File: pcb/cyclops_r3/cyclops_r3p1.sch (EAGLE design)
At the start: 70 parts, among them Q1 SUM11006, Q2 IRF510, U1 MCP4921, U2 317-N, U3 ADR03, U4 OP1177, U5 LM324N, U6 ZXTD45, U8 TLV3701CDBVT

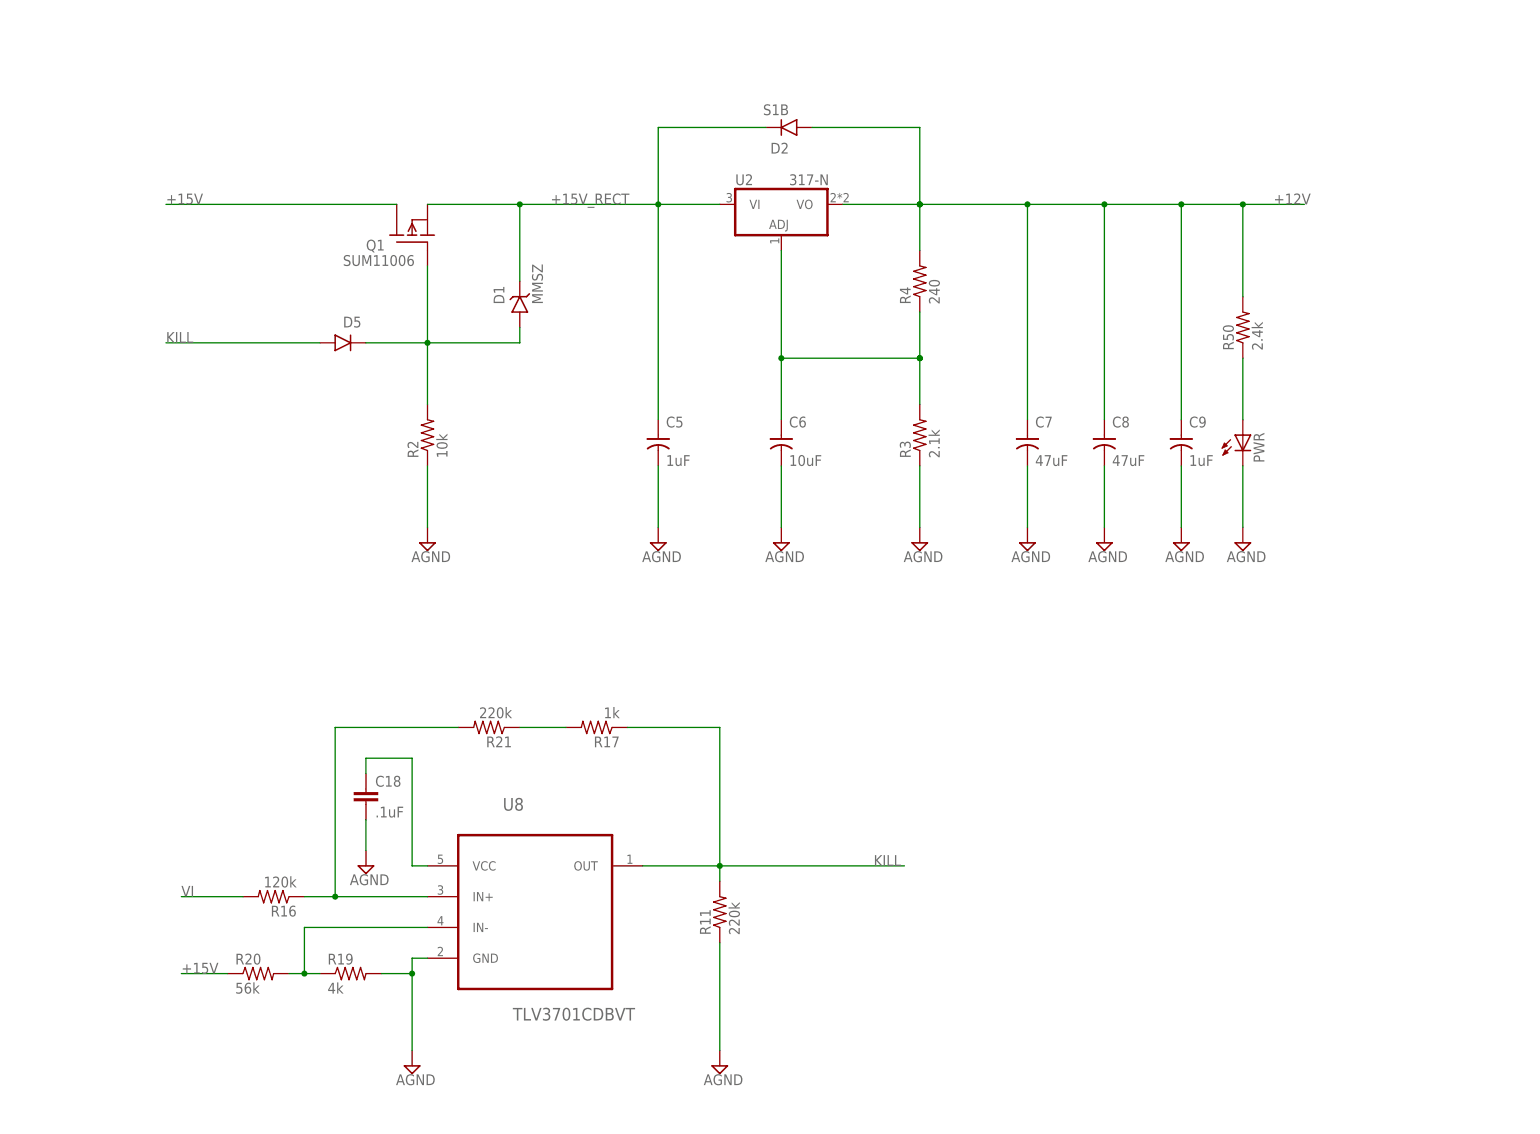
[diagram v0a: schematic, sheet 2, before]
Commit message: Modifications to overcurrent protection allow 2A max, and lights alarm LED.
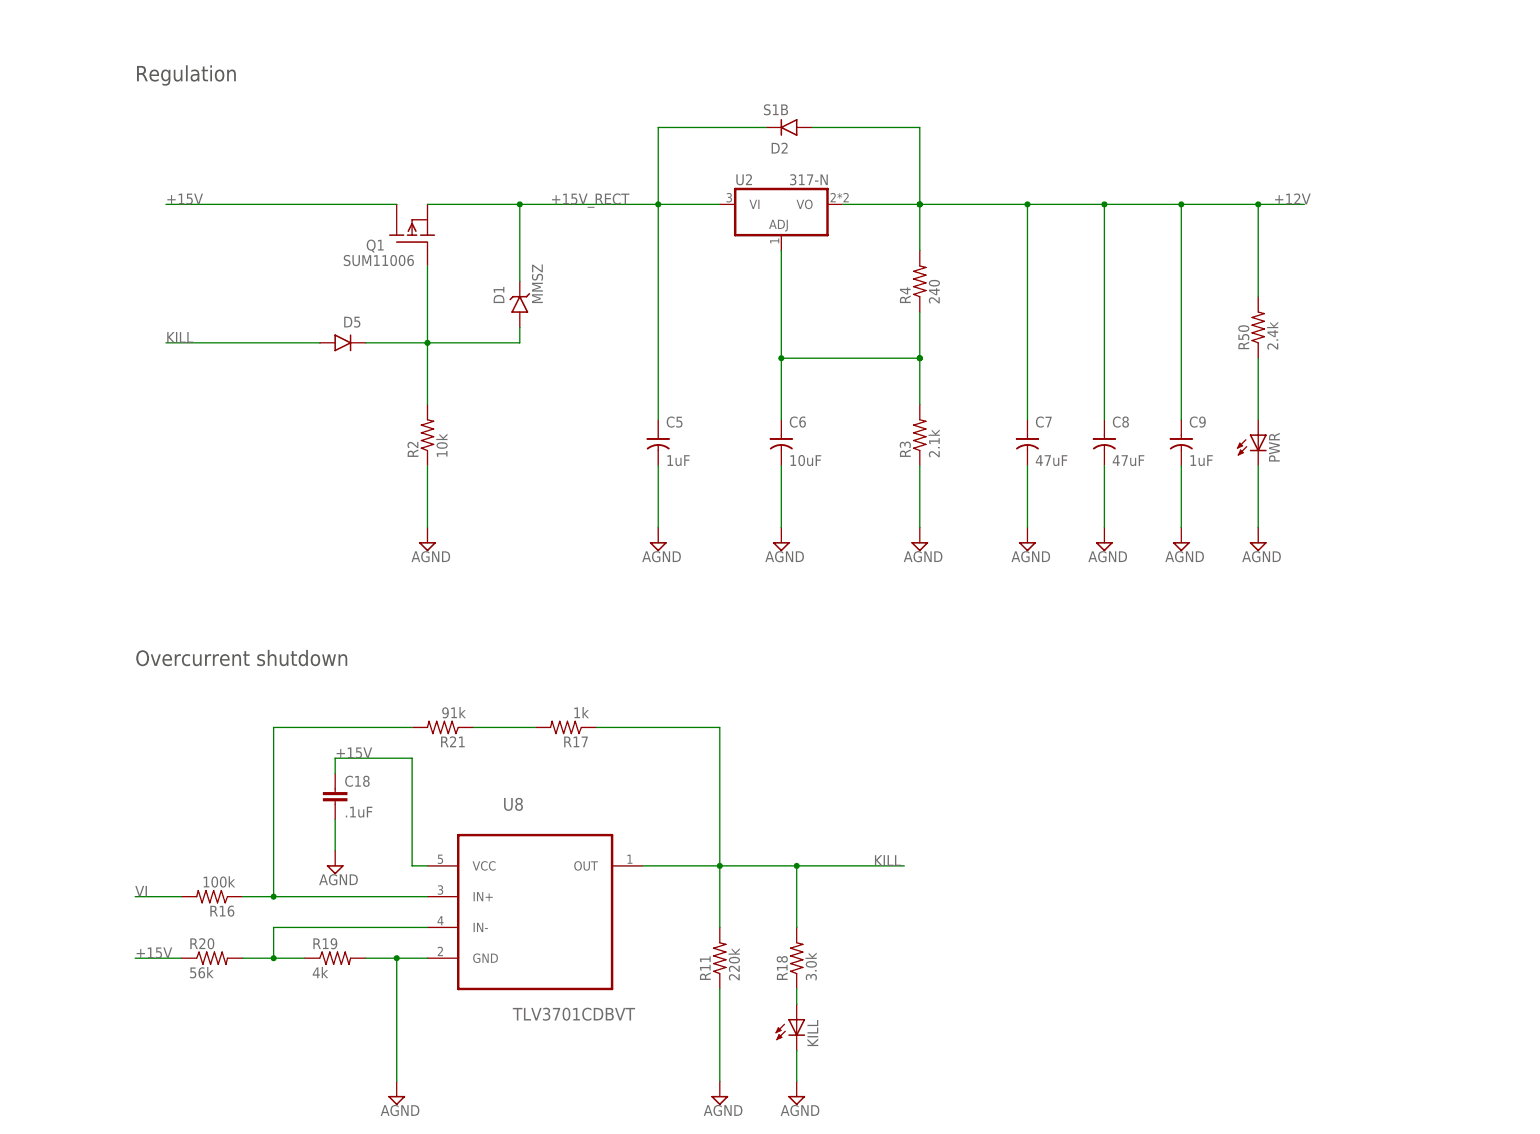
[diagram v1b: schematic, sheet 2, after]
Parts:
- added KILL: (no value), cyclops:LEDYELLOW_0805
- added R18: 3.0k, cyclops:R_0603
- R16: value 120k -> 100k
- R21: value 220k -> 91k
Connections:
- new net N$11: KILL.A, R18.1
- net GND: now also KILL.C
- net KILL: now also R18.2
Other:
- note added: "Board Temperature"
- note added: "I/O and DAC"
- note added: "Overcurrent shutdown"
- note added: "Reference voltage"
- note added: "Regulation"
- moved on the sheet: C18, PWR, R11, R16, R17, R19, R20, R21, R50

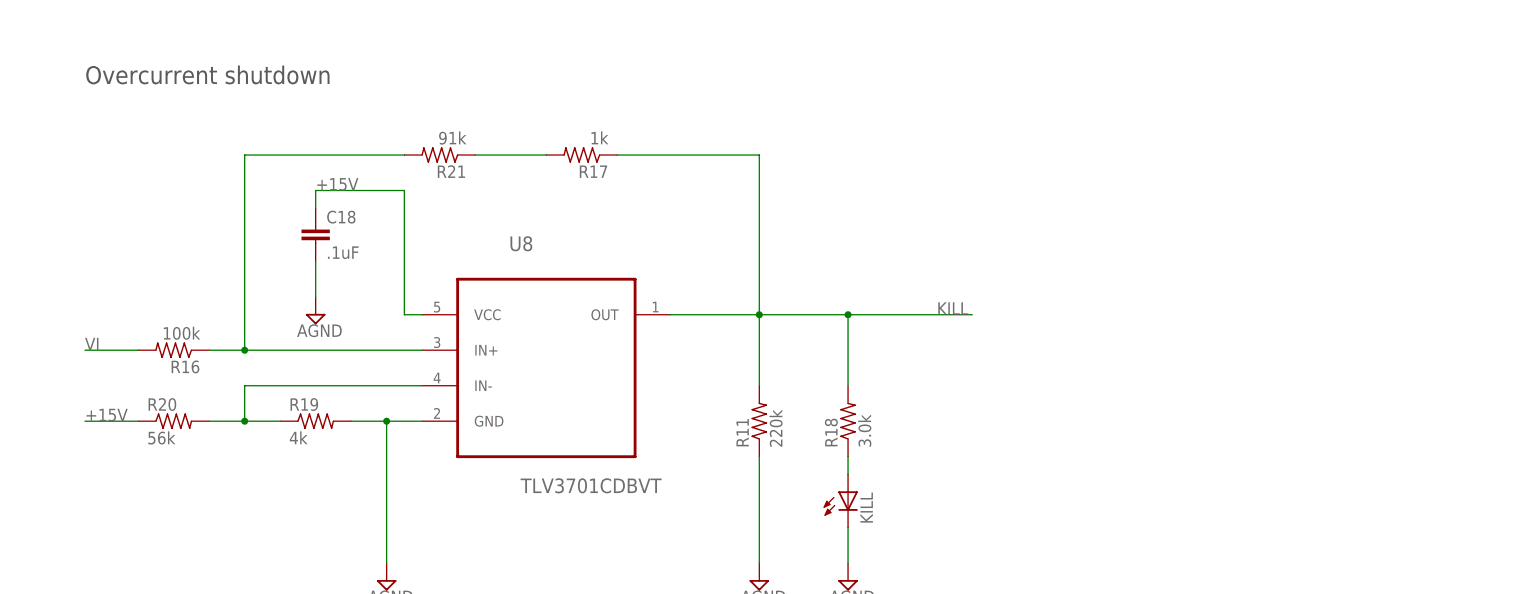
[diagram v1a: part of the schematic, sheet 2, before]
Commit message: Started implementing the over curren protection circuit on the board.
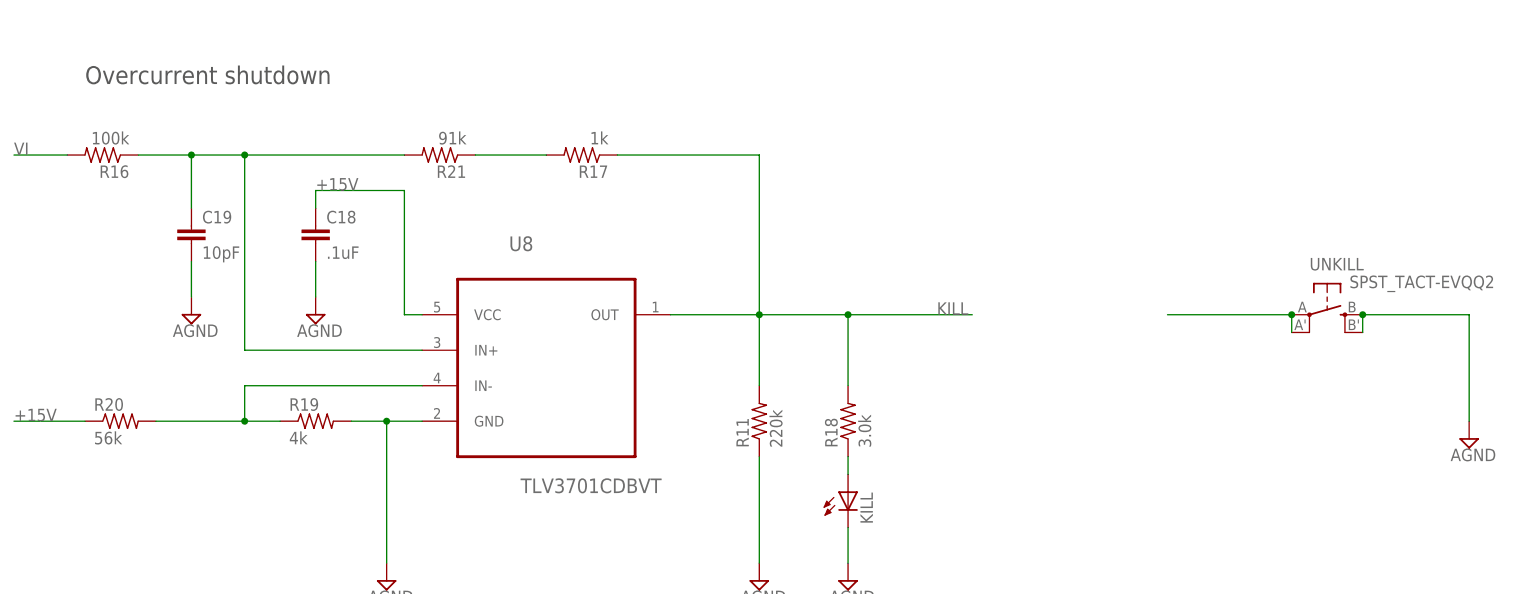
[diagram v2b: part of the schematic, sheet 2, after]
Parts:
- added C19: 10pF, cyclops:C_0603
- added UNKILL: SPST_TACT-EVQQ2, cyclops:SPST_TACT-EVQQ2
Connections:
- removed net N$14: R16.1, R21.2, U8.IN+
- new net COMP+: C19.1, R16.1, R21.2, U8.IN+, UNKILL.P, UNKILL.P1
- net AGND: now also UNKILL.S, UNKILL.S1
- net GND: now also C19.2
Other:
- moved on the sheet: R16, R20
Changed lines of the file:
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@@
 <part name="KILL" library="cyclops" deviceset="LED" device="_0805" technology="YELLOW"/>
 <part name="SUPPLY44" library="supply2" deviceset="AGND" device=""/>
+<part name="C19" library="cyclops" deviceset="C" device="_0603" value="10pF"/>
+<part name="SUPPLY45" library="cyclops" deviceset="AGND" device=""/>
+<part name="UNKILL" library="cyclops" deviceset="SPST_TACT" device="-EVQQ2"/>
+<part name="SUPPLY46" library="supply2" deviceset="AGND" device=""/>
 </parts>
 <sheets>
@@
 <attribute name="VALUE" x="-44.45" y="-99.822" size="1.778" layer="96"/>
 </instance>
-<instance part="R20" gate="R" x="-60.96" y="-96.52" smashed="yes">
-<attribute name="NAME" x="-64.77" y="-95.0214" size="1.778" layer="95"/>
-<attribute name="VALUE" x="-64.77" y="-99.822" size="1.778" layer="96"/>
+<instance part="R20" gate="R" x="-68.58" y="-96.52" smashed="yes">
+<attribute name="NAME" x="-72.39" y="-95.0214" size="1.778" layer="95"/>
+<attribute name="VALUE" x="-72.39" y="-99.822" size="1.778" layer="96"/>
 </instance>
 <instance part="R21" gate="R" x="-22.86" y="-58.42" smashed="yes" rot="R180">
@@
 <attribute name="VALUE" x="-19.05" y="-55.118" size="1.778" layer="96" rot="R180"/>
 </instance>
-<instance part="R16" gate="R" x="-60.96" y="-86.36" smashed="yes" rot="R180">
-<attribute name="NAME" x="-57.15" y="-87.8586" size="1.778" layer="95" rot="R180"/>
-<attribute name="VALUE" x="-57.15" y="-83.058" size="1.778" layer="96" rot="R180"/>
+<instance part="R16" gate="R" x="-71.12" y="-58.42" smashed="yes" rot="R180">
+<attribute name="NAME" x="-67.31" y="-59.9186" size="1.778" layer="95" rot="R180"/>
+<attribute name="VALUE" x="-67.31" y="-55.118" size="1.778" layer="96" rot="R180"/>
 </instance>
 <instance part="SUPPLY41" gate="G$1" x="22.86" y="-119.38"/>
@@
 <instance part="KILL" gate="G$1" x="35.56" y="-106.68"/>
 <instance part="SUPPLY44" gate="G$1" x="35.56" y="-119.38"/>
+<instance part="C19" gate="C" x="-58.42" y="-68.58"/>
+<instance part="SUPPLY45" gate="G$1" x="-58.42" y="-81.28"/>
+<instance part="UNKILL" gate="G$1" x="104.14" y="-81.28" rot="R270"/>
+<instance part="SUPPLY46" gate="G$1" x="124.46" y="-99.06"/>
 </instances>
 <busses>
@@
 <segment>
 <pinref part="R20" gate="R" pin="1"/>
-<wire x1="-66.04" y1="-96.52" x2="-73.66" y2="-96.52" width="0.1524" layer="91"/>
-<label x="-73.66" y="-96.52" size="1.778" layer="95"/>
+<wire x1="-73.66" y1="-96.52" x2="-83.82" y2="-96.52" width="0.1524" layer="91"/>
+<label x="-83.82" y="-96.52" size="1.778" layer="95"/>
 </segment>
 <segment>
@@
 <wire x1="35.56" y1="-111.76" x2="35.56" y2="-116.84" width="0.1524" layer="91"/>
 </segment>
+<segment>
+<pinref part="SUPPLY45" gate="G$1" pin="AGND"/>
+<pinref part="C19" gate="C" pin="2"/>
+<wire x1="-58.42" y1="-78.74" x2="-58.42" y2="-73.66" width="0.1524" layer="91"/>
+</segment>
 </net>
 <net name="N$18" class="0">
@@
 </segment>
 </net>
-<net name="N$14" class="0">
-<segment>
-<pinref part="U8" gate="A" pin="IN+"/>
-<wire x1="-25.4" y1="-86.36" x2="-50.8" y2="-86.36" width="0.1524" layer="91"/>
-<wire x1="-50.8" y1="-86.36" x2="-50.8" y2="-58.42" width="0.1524" layer="91"/>
-<wire x1="-50.8" y1="-58.42" x2="-27.94" y2="-58.42" width="0.1524" layer="91"/>
-<pinref part="R16" gate="R" pin="1"/>
-<wire x1="-55.88" y1="-86.36" x2="-50.8" y2="-86.36" width="0.1524" layer="91"/>
-<junction x="-50.8" y="-86.36"/>
-<pinref part="R21" gate="R" pin="2"/>
-</segment>
-</net>
 <net name="N$5" class="0">
 <segment>
 <pinref part="R20" gate="R" pin="2"/>
 <pinref part="R19" gate="R" pin="1"/>
-<wire x1="-55.88" y1="-96.52" x2="-50.8" y2="-96.52" width="0.1524" layer="91"/>
+<wire x1="-63.5" y1="-96.52" x2="-50.8" y2="-96.52" width="0.1524" layer="91"/>
 <wire x1="-50.8" y1="-96.52" x2="-45.72" y2="-96.52" width="0.1524" layer="91"/>
 <wire x1="-50.8" y1="-96.52" x2="-50.8" y2="-91.44" width="0.1524" layer="91"/>
@@
 <segment>
 <pinref part="R16" gate="R" pin="2"/>
-<wire x1="-66.04" y1="-86.36" x2="-73.66" y2="-86.36" width="0.1524" layer="91"/>
-<label x="-73.66" y="-86.36" size="1.778" layer="95"/>
+<wire x1="-76.2" y1="-58.42" x2="-83.82" y2="-58.42" width="0.1524" layer="91"/>
+<label x="-83.82" y="-58.42" size="1.778" layer="95"/>
 </segment>
 </net>
@@
 </segment>
 </net>
+<net name="COMP+" class="0">
+<segment>
+<pinref part="UNKILL" gate="G$1" pin="P"/>
+<wire x1="81.28" y1="-81.28" x2="99.06" y2="-81.28" width="0.1524" layer="91"/>
+<pinref part="UNKILL" gate="G$1" pin="P1"/>
+<wire x1="99.06" y1="-81.28" x2="99.06" y2="-83.82" width="0.1524" layer="91"/>
+<junction x="99.06" y="-81.28"/>
+</segment>
+<segment>
+<pinref part="U8" gate="A" pin="IN+"/>
+<wire x1="-25.4" y1="-86.36" x2="-50.8" y2="-86.36" width="0.1524" layer="91"/>
+<wire x1="-50.8" y1="-86.36" x2="-50.8" y2="-58.42" width="0.1524" layer="91"/>
+<wire x1="-50.8" y1="-58.42" x2="-27.94" y2="-58.42" width="0.1524" layer="91"/>
+<pinref part="R16" gate="R" pin="1"/>
+<wire x1="-66.04" y1="-58.42" x2="-58.42" y2="-58.42" width="0.1524" layer="91"/>
+<junction x="-50.8" y="-58.42"/>
+<pinref part="R21" gate="R" pin="2"/>
+<pinref part="C19" gate="C" pin="1"/>
+<wire x1="-58.42" y1="-58.42" x2="-50.8" y2="-58.42" width="0.1524" layer="91"/>
+<wire x1="-58.42" y1="-66.04" x2="-58.42" y2="-58.42" width="0.1524" layer="91"/>
+<junction x="-58.42" y="-58.42"/>
+</segment>
+</net>
+<net name="AGND" class="0">
+<segment>
+<pinref part="UNKILL" gate="G$1" pin="S1"/>
+<pinref part="UNKILL" gate="G$1" pin="S"/>
+<wire x1="109.22" y1="-83.82" x2="109.22" y2="-81.28" width="0.1524" layer="91"/>
+<wire x1="109.22" y1="-81.28" x2="124.46" y2="-81.28" width="0.1524" layer="91"/>
+<junction x="109.22" y="-81.28"/>
+<wire x1="124.46" y1="-81.28" x2="124.46" y2="-96.52" width="0.1524" layer="91"/>
+<pinref part="SUPPLY46" gate="G$1" pin="AGND"/>
+</segment>
+</net>

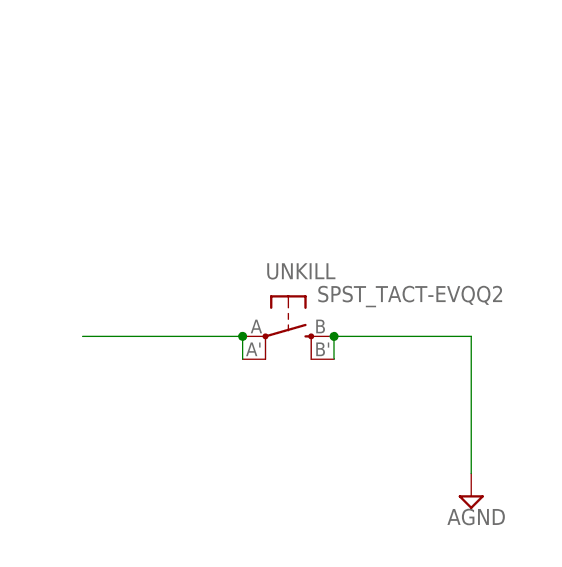
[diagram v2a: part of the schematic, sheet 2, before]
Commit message: Several changes to board layout. Also, some new design notes.
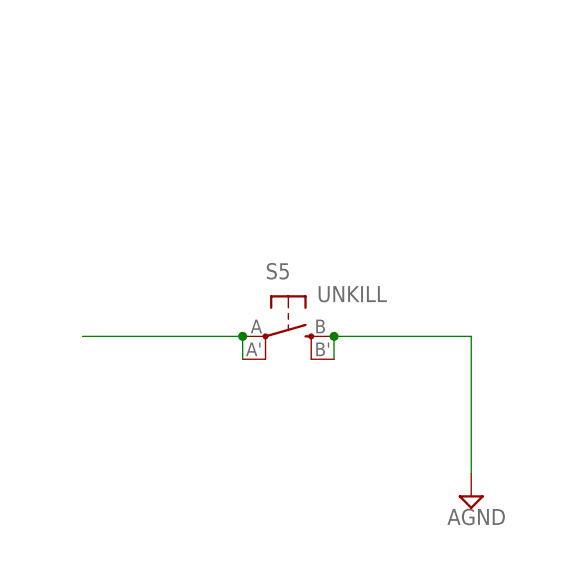
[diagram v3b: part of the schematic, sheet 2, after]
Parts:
- S5: value SPST_TACT-EVQQ2 -> UNKILL
- renumbered UNKILL to S5
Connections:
- removed net AGND: BIAS.E, C17.2, S5.S, S5.S1
- net GND: now also BIAS.E, C17.2, S5.S, S5.S1
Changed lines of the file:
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@@
 <part name="C19" library="cyclops" deviceset="C" device="_0603" value="10pF"/>
 <part name="SUPPLY45" library="cyclops" deviceset="AGND" device=""/>
-<part name="UNKILL" library="cyclops" deviceset="SPST_TACT" device="-EVQQ2"/>
+<part name="S5" library="cyclops" deviceset="SPST_TACT" device="-EVQQ2" value="UNKILL"/>
 <part name="SUPPLY46" library="supply2" deviceset="AGND" device=""/>
 </parts>
@@
 <instance part="C19" gate="C" x="-58.42" y="-68.58"/>
 <instance part="SUPPLY45" gate="G$1" x="-58.42" y="-81.28"/>
-<instance part="UNKILL" gate="G$1" x="104.14" y="-81.28" rot="R270"/>
+<instance part="S5" gate="G$1" x="104.14" y="-81.28" rot="R270"/>
 <instance part="SUPPLY46" gate="G$1" x="124.46" y="-99.06"/>
 </instances>
@@
 <wire x1="-58.42" y1="-78.74" x2="-58.42" y2="-73.66" width="0.1524" layer="91"/>
 </segment>
+<segment>
+<pinref part="S5" gate="G$1" pin="S1"/>
+<pinref part="S5" gate="G$1" pin="S"/>
+<wire x1="109.22" y1="-83.82" x2="109.22" y2="-81.28" width="0.1524" layer="91"/>
+<wire x1="109.22" y1="-81.28" x2="124.46" y2="-81.28" width="0.1524" layer="91"/>
+<junction x="109.22" y="-81.28"/>
+<wire x1="124.46" y1="-81.28" x2="124.46" y2="-96.52" width="0.1524" layer="91"/>
+<pinref part="SUPPLY46" gate="G$1" pin="AGND"/>
+</segment>
 </net>
 <net name="N$18" class="0">
@@
 <net name="COMP+" class="0">
 <segment>
-<pinref part="UNKILL" gate="G$1" pin="P"/>
+<pinref part="S5" gate="G$1" pin="P"/>
 <wire x1="81.28" y1="-81.28" x2="99.06" y2="-81.28" width="0.1524" layer="91"/>
-<pinref part="UNKILL" gate="G$1" pin="P1"/>
+<pinref part="S5" gate="G$1" pin="P1"/>
 <wire x1="99.06" y1="-81.28" x2="99.06" y2="-83.82" width="0.1524" layer="91"/>
 <junction x="99.06" y="-81.28"/>
@@
 <wire x1="-58.42" y1="-66.04" x2="-58.42" y2="-58.42" width="0.1524" layer="91"/>
 <junction x="-58.42" y="-58.42"/>
-</segment>
-</net>
-<net name="AGND" class="0">
-<segment>
-<pinref part="UNKILL" gate="G$1" pin="S1"/>
-<pinref part="UNKILL" gate="G$1" pin="S"/>
-<wire x1="109.22" y1="-83.82" x2="109.22" y2="-81.28" width="0.1524" layer="91"/>
-<wire x1="109.22" y1="-81.28" x2="124.46" y2="-81.28" width="0.1524" layer="91"/>
-<junction x="109.22" y="-81.28"/>
-<wire x1="124.46" y1="-81.28" x2="124.46" y2="-96.52" width="0.1524" layer="91"/>
-<pinref part="SUPPLY46" gate="G$1" pin="AGND"/>
 </segment>
 </net>
@@
 <pinref part="SUPPLY38" gate="G$1" pin="AGND"/>
 </segment>
+<segment>
+<pinref part="BIAS" gate="1" pin="E"/>
+<pinref part="SUPPLY39" gate="G$1" pin="AGND"/>
+<wire x1="50.8" y1="116.84" x2="50.8" y2="114.3" width="0.1524" layer="91"/>
+<pinref part="C17" gate="C" pin="2"/>
+<wire x1="50.8" y1="114.3" x2="50.8" y2="109.22" width="0.1524" layer="91"/>
+<wire x1="66.04" y1="121.92" x2="66.04" y2="114.3" width="0.1524" layer="91"/>
+<wire x1="66.04" y1="114.3" x2="50.8" y2="114.3" width="0.1524" layer="91"/>
+<junction x="50.8" y="114.3"/>
+</segment>
 </net>
 <net name="+12V" class="1">
@@
 </segment>
 </net>
-<net name="AGND" class="0">
-<segment>
-<pinref part="BIAS" gate="1" pin="E"/>
-<pinref part="SUPPLY39" gate="G$1" pin="AGND"/>
-<wire x1="50.8" y1="116.84" x2="50.8" y2="114.3" width="0.1524" layer="91"/>
-<pinref part="C17" gate="C" pin="2"/>
-<wire x1="50.8" y1="114.3" x2="50.8" y2="109.22" width="0.1524" layer="91"/>
-<wire x1="66.04" y1="121.92" x2="66.04" y2="114.3" width="0.1524" layer="91"/>
-<wire x1="66.04" y1="114.3" x2="50.8" y2="114.3" width="0.1524" layer="91"/>
-<junction x="50.8" y="114.3"/>
-</segment>
-</net>
